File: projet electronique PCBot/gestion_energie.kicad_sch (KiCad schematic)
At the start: 4 parts, among them U2 BU33SD5WG-TR, U3 BQ25896RTWR

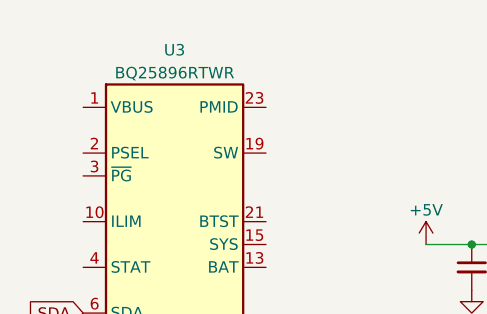
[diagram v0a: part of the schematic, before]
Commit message: Ajout de la feuille hiérarchique moteur
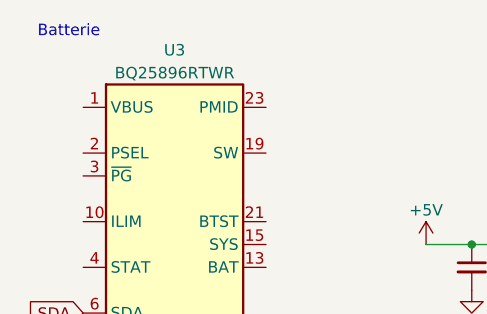
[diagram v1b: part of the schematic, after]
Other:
- note added: "Batterie"
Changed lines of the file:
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@@
+    (effects (font (size 1.27 1.27)) (justify left bottom))
+  )
+  (text "Batterie" (at 96.52 59.69 0)
     (effects (font (size 1.27 1.27)) (justify left bottom))
   )

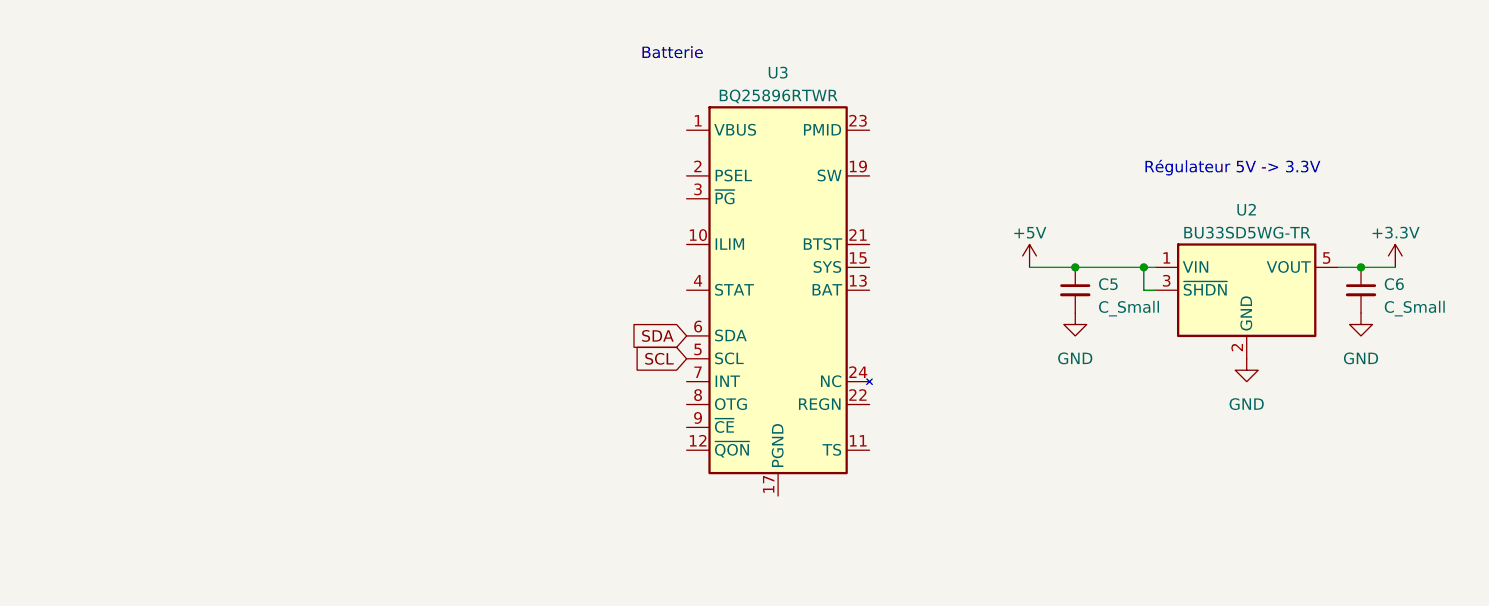
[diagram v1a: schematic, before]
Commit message: Modification des feuilles hiérarchiques et le main
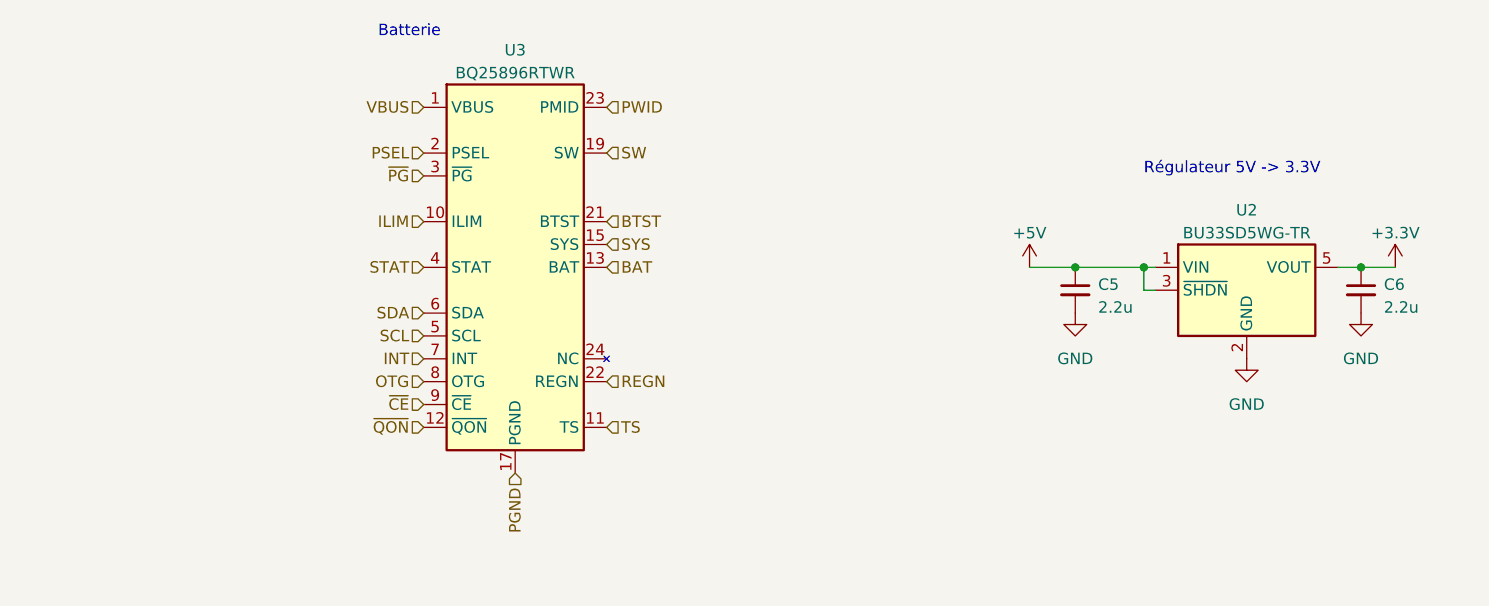
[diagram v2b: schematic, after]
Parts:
- C5, C6: value C_Small -> 2.2u
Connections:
- net VBUS: now reaches U3.1 (VBUS)
- net ILIM: now reaches U3.10 (ILIM)
- net TS: now reaches U3.11 (TS)
- net ~{QON}: now reaches U3.12 (~{QON})
- net BAT: now reaches U3.13 (BAT), U3.14 (BAT)
- net SYS: now reaches U3.15 (SYS), U3.16 (SYS)
- net PGND: now reaches U3.17 (PGND), U3.18 (PGND), U3.25 (PGND)
- net SW: now reaches U3.19 (SW), U3.20 (SW)
- net PSEL: now reaches U3.2 (PSEL)
- net BTST: now reaches U3.21 (BTST)
- net REGN: now reaches U3.22 (REGN)
- net PWID: now reaches U3.23 (PMID)
- net ~{PG}: now reaches U3.3 (~{PG})
- net STAT: now reaches U3.4 (STAT)
- net INT: now reaches U3.7 (INT)
- net OTG: now reaches U3.8 (OTG)
- net ~{CE}: now reaches U3.9 (~{CE})
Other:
- moved on the sheet: U3
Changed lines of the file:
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@@
     (effects (font (size 1.27 1.27)) (justify left bottom))
   )
-  (text "Batterie" (at 96.52 59.69 0)
+  (text "Batterie" (at 67.31 57.15 0)
     (effects (font (size 1.27 1.27)) (justify left bottom))
   )
-  (global_label "SDA" (shape input) (at 101.6 90.17 180) (fields_autoplaced)
-    (effects (font (size 1.27 1.27)) (justify right))
-    (property "Intersheetrefs" "${INTERSHEET_REFS}" (at 95.1261 90.17 0)
-      (effects (font (size 1.27 1.27)) (justify right) hide)
-    )
-  )
-  (global_label "SCL" (shape input) (at 101.6 92.71 180) (fields_autoplaced)
-    (effects (font (size 1.27 1.27)) (justify right))
-    (property "Intersheetrefs" "${INTERSHEET_REFS}" (at 95.1866 92.71 0)
-      (effects (font (size 1.27 1.27)) (justify right) hide)
-    )
+  (hierarchical_label "SDA" (shape input) (at 72.39 87.63 180) (fields_autoplaced)
+    (effects (font (size 1.27 1.27)) (justify right))
+  )
+  (hierarchical_label "ILIM" (shape input) (at 72.39 77.47 180) (fields_autoplaced)
+    (effects (font (size 1.27 1.27)) (justify right))
+  )
+  (hierarchical_label "BTST" (shape input) (at 92.71 77.47 0) (fields_autoplaced)
+    (effects (font (size 1.27 1.27)) (justify left))
+  )
+  (hierarchical_label "STAT" (shape input) (at 72.39 82.55 180) (fields_autoplaced)
+    (effects (font (size 1.27 1.27)) (justify right))
+  )
+  (hierarchical_label "TS" (shape input) (at 92.71 100.33 0) (fields_autoplaced)
+    (effects (font (size 1.27 1.27)) (justify left))
+  )
+  (hierarchical_label "INT" (shape input) (at 72.39 92.71 180) (fields_autoplaced)
+    (effects (font (size 1.27 1.27)) (justify right))
+  )
+  (hierarchical_label "PGND" (shape input) (at 82.55 105.41 270) (fields_autoplaced)
+    (effects (font (size 1.27 1.27)) (justify right))
+  )
+  (hierarchical_label "PWID" (shape input) (at 92.71 64.77 0) (fields_autoplaced)
+    (effects (font (size 1.27 1.27)) (justify left))
+  )
+  (hierarchical_label "PSEL" (shape input) (at 72.39 69.85 180) (fields_autoplaced)
+    (effects (font (size 1.27 1.27)) (justify right))
+  )
+  (hierarchical_label "VBUS" (shape input) (at 72.39 64.77 180) (fields_autoplaced)
+    (effects (font (size 1.27 1.27)) (justify right))
+  )
+  (hierarchical_label "~{QON}" (shape input) (at 72.39 100.33 180) (fields_autoplaced)
+    (effects (font (size 1.27 1.27)) (justify right))
+  )
+  (hierarchical_label "SYS" (shape input) (at 92.71 80.01 0) (fields_autoplaced)
+    (effects (font (size 1.27 1.27)) (justify left))
+  )
+  (hierarchical_label "~{CE}" (shape input) (at 72.39 97.79 180) (fields_autoplaced)
+    (effects (font (size 1.27 1.27)) (justify right))
+  )
+  (hierarchical_label "~{PG}" (shape input) (at 72.39 72.39 180) (fields_autoplaced)
+    (effects (font (size 1.27 1.27)) (justify right))
+  )
+  (hierarchical_label "SCL" (shape input) (at 72.39 90.17 180) (fields_autoplaced)
+    (effects (font (size 1.27 1.27)) (justify right))
+  )
+  (hierarchical_label "SW" (shape input) (at 92.71 69.85 0) (fields_autoplaced)
+    (effects (font (size 1.27 1.27)) (justify left))
+  )
+  (hierarchical_label "BAT" (shape input) (at 92.71 82.55 0) (fields_autoplaced)
+    (effects (font (size 1.27 1.27)) (justify left))
+  )
+  (hierarchical_label "OTG" (shape input) (at 72.39 95.25 180) (fields_autoplaced)
+    (effects (font (size 1.27 1.27)) (justify right))
+  )
+  (hierarchical_label "REGN" (shape input) (at 92.71 95.25 0) (fields_autoplaced)
+    (effects (font (size 1.27 1.27)) (justify left))
   )
   (symbol (lib_id "Regulator_Linear:MCP1802x-xx02xOT") (at 163.83 85.09 0) (unit 1)
@@
       (effects (font (size 1.27 1.27)) (justify left))
     )
-    (property "Value" "C_Small" (at 147.32 87.0013 0)
+    (property "Value" "2.2u" (at 147.32 87.0013 0)
       (effects (font (size 1.27 1.27)) (justify left))
     )
@@
       (effects (font (size 1.27 1.27)) (justify left))
     )
-    (property "Value" "C_Small" (at 179.07 87.0013 0)
+    (property "Value" "2.2u" (at 179.07 87.0013 0)
       (effects (font (size 1.27 1.27)) (justify left))
     )
@@
     )
   )
-  (symbol (lib_id "pcbot_lib:BQ25896RTW") (at 111.76 85.09 0) (unit 1)
-    (in_bom yes) (on_board yes) (dnp no) (fields_autoplaced)
-    (property "Reference" "U3" (at 111.76 60.96 0)
-      (effects (font (size 1.27 1.27)))
-    )
-    (property "Value" "BQ25896RTWR" (at 111.76 63.5 0)
-      (effects (font (size 1.27 1.27)))
-    )
-    (property "Footprint" "Package_DFN_QFN:Texas_S-PWQFN-N24_EP2.7x2.7mm_ThermalVias" (at 109.22 59.69 0)
-      (effects (font (size 1.27 1.27)) hide)
-    )
-    (property "Datasheet" "http://www.ti.com/lit/ds/symlink/bq25895.pdf" (at 106.68 64.77 0)
-      (effects (font (size 1.27 1.27)) hide)
-    )
+  (symbol (lib_id "pcbot_lib:BQ25896RTW") (at 82.55 82.55 0) (unit 1)
+    (in_bom yes) (on_board yes) (dnp no) (fields_autoplaced)
+    (property "Reference" "U3" (at 82.55 58.42 0)
+      (effects (font (size 1.27 1.27)))
+    )
+    (property "Value" "BQ25896RTWR" (at 82.55 60.96 0)
+      (effects (font (size 1.27 1.27)))
+    )
+    (property "Footprint" "Package_DFN_QFN:Texas_S-PWQFN-N24_EP2.7x2.7mm_ThermalVias" (at 80.01 57.15 0)
+      (effects (font (size 1.27 1.27)) hide)
+    )
+    (property "Datasheet" "http://www.ti.com/lit/ds/symlink/bq25895.pdf" (at 77.47 62.23 0)
+      (effects (font (size 1.27 1.27)) hide)
+    )

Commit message: ajout de la feuille connecteurs
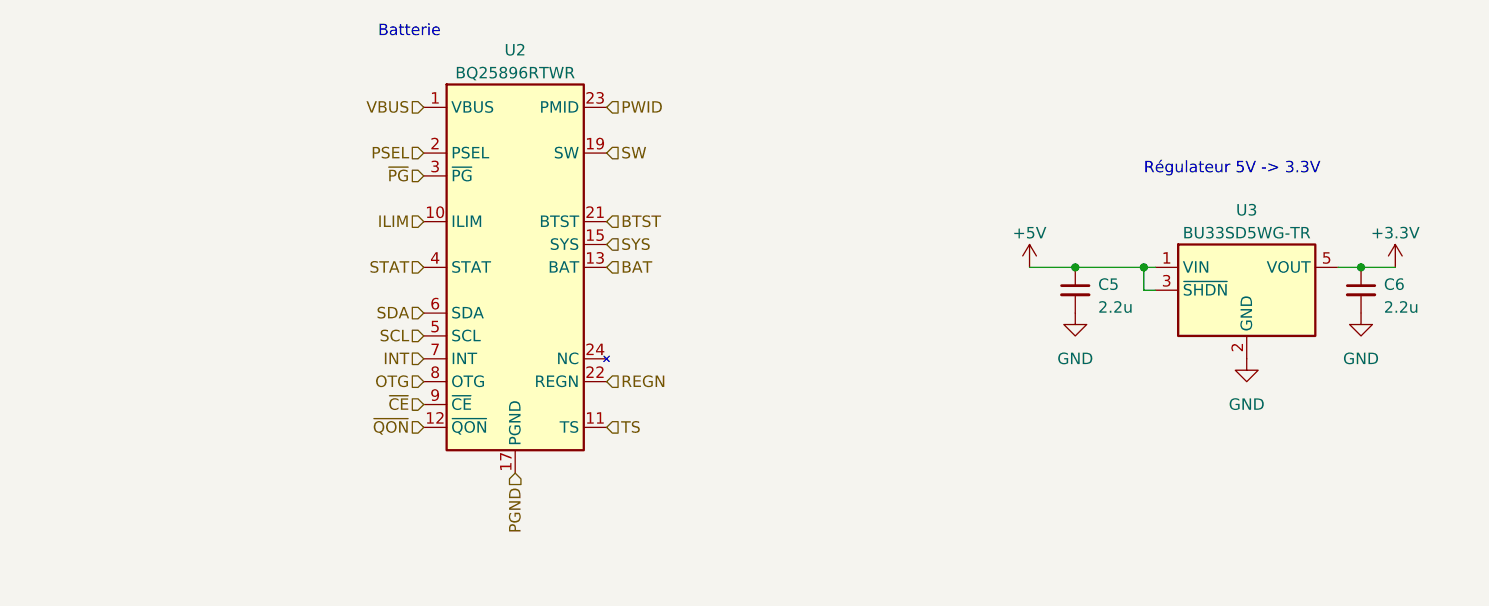
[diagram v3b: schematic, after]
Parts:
- renumbered U3 to U2, U2 to U3

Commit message: modification gestion_energie
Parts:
- added C7, C8: C_Small, symbol Device:C_Small
- added L1: L_Small, symbol Device:L_Small
- added R1, R2: 10k, symbol Device:R_Small
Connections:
- net GND: now also C7.2, R1.2
- net BAT: no longer names the net of U2.13 (BAT), U2.14 (BAT)
- net BAT: now also C7.1
- net PWID: no longer names the net of U2.23 (PMID)
- net PWID: now also L1.1
- net REGN: no longer names the net of U2.22 (REGN)
- net REGN: now also C8.1, R2.1
- net TS: no longer names the net of U2.11 (TS)
- net TS: now also C8.2, R1.1, R2.2
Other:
- note added: "BMS"
- note added: "Lier VBUS à USB (3.9V-14V à 3A) avec OTG 5V à 2A"
- note removed: "Batterie"

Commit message: modif
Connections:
- net GND: now also L1.2
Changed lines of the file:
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@@
+	(wire
+		(pts
+			(xy 105.41 64.77) (xy 100.33 64.77)
+		)
+		(stroke
+			(width 0)
+			(type default)
+		)
+	)
 	(wire
 		(pts
@@
 					(unit 1)
 				)
+			)
+		)
+	)
+	(symbol
+		(lib_name "GND_2")
+		(lib_id "power:GND")
+		(at 105.41 64.77 0)
+		(unit 1)
+		(exclude_from_sim no)
+		(in_bom yes)
+		(on_board yes)
+		(dnp no)
+		(fields_autoplaced yes)
+		(property "Reference" "#PWR023"
+			(at 105.41 71.12 0)
+			(effects
+				(font
+					(size 1.27 1.27)
+				)
+				(hide yes)
+			)
+		)
+		(property "Value" "GND"
+			(at 105.41 69.85 0)
+			(effects
+				(font
+					(size 1.27 1.27)
+				)
+			)
+		)
+		(property "Footprint" ""
+			(at 105.41 64.77 0)
+			(effects
+				(font
+					(size 1.27 1.27)
+				)
+				(hide yes)
+			)
+		)
+		(property "Datasheet" ""
+			(at 105.41 64.77 0)
+			(effects
+				(font
+					(size 1.27 1.27)
+				)
+				(hide yes)
+			)
+		)
+		(property "Description" "Power symbol creates a global label with name \"GND\" , ground"
+			(at 105.41 64.77 0)
+			(effects
+				(font
+					(size 1.27 1.27)
+				)
+				(hide yes)
+			)
+		)
+		(pin "1"
+		)
+		(instances
+			(project ""
+				(path "/210be09d-86cd-4faa-bb91-cc54c5972517/d457b8fa-dc83-43ee-b672-fc417651a09a"
+					(reference "#PWR023")
+					(unit 1)
+				)
